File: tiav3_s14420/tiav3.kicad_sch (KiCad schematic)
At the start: 21 parts, among them J1 SSQ-103-01-G-D, J2 Conn_Coaxial, U1 OPA847IDBVT

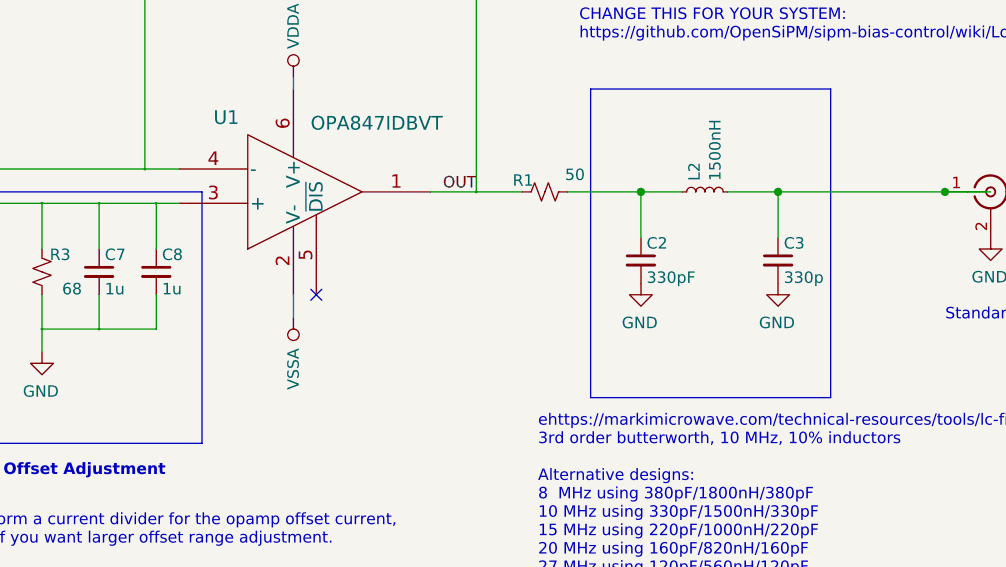
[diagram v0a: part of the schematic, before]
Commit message: Switch all TIA boards to 0603 for the low pass inductor
0402 is fine for higher cutoffs but its hard to find >1000nH in 0402 without having high resistance.
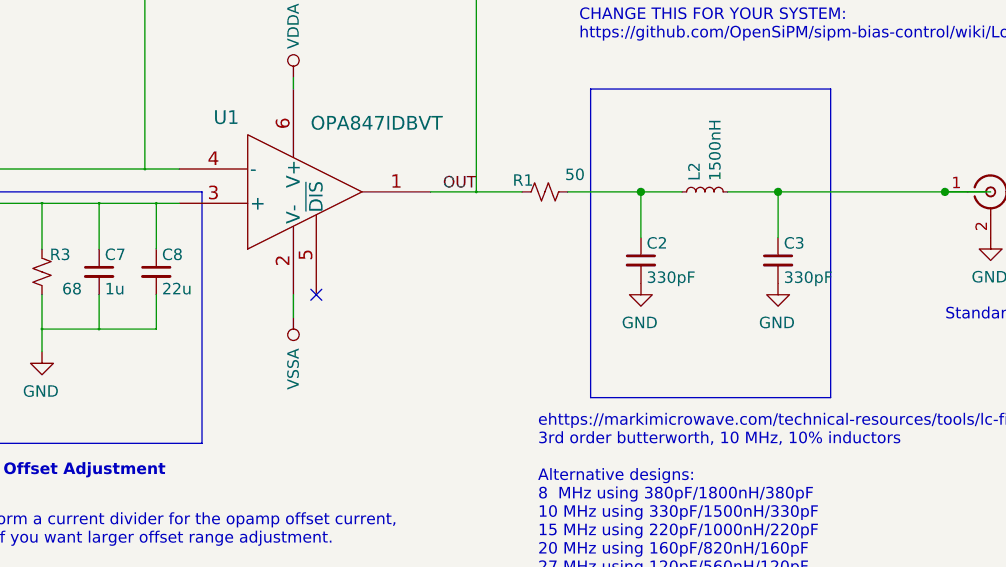
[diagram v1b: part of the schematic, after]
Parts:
- C1, C4: footprint Resistor_SMD:R_1206_3216Metric -> Capacitor_SMD:C_1206_3216Metric_Pad1.33x1.80mm_HandSolder
- C2: footprint Capacitor_SMD:C_0402_1005Metric -> Capacitor_SMD:C_0402_1005Metric_Pad0.74x0.62mm_HandSolder
- C3: value 330p -> 330pF; footprint Capacitor_SMD:C_0402_1005Metric -> Capacitor_SMD:C_0402_1005Metric_Pad0.74x0.62mm_HandSolder
- C8: value 1u -> 22u; footprint Capacitor_SMD:C_0402_1005Metric -> Capacitor_SMD:C_0603_1608Metric
- L2: footprint Inductor_SMD:L_0402_1005Metric -> Inductor_SMD:L_0603_1608Metric
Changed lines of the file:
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@@
 			)
 		)
-		(property "Footprint" "Resistor_SMD:R_1206_3216Metric"
+		(property "Footprint" "Capacitor_SMD:C_1206_3216Metric_Pad1.33x1.80mm_HandSolder"
 			(at 71.12 101.6 0)
 			(effects
@@
 			)
 		)
-		(property "Value" "1u"
+		(property "Value" "22u"
 			(at 172.085 121.285 0)
 			(effects
@@
 			)
 		)
-		(property "Footprint" "Capacitor_SMD:C_0402_1005Metric"
+		(property "Footprint" "Capacitor_SMD:C_0603_1608Metric"
 			(at 171.45 119.38 0)
 			(effects
@@
 			)
 		)
-		(property "Datasheet" " ~"
+		(property "Datasheet" "~"
 			(at 264.16 110.49 0)
 			(effects
@@
 			)
 		)
-		(property "Footprint" "Inductor_SMD:L_0402_1005Metric"
+		(property "Footprint" "Inductor_SMD:L_0603_1608Metric"
 			(at 232.41 110.49 0)
 			(effects
@@
 			)
 		)
-		(property "Footprint" "Capacitor_SMD:C_0402_1005Metric"
+		(property "Footprint" "Capacitor_SMD:C_0402_1005Metric_Pad0.74x0.62mm_HandSolder"
 			(at 225.298 118.11 0)
 			(effects
@@
 			)
 		)
-		(property "Footprint" "Resistor_SMD:R_1206_3216Metric"
+		(property "Footprint" "Capacitor_SMD:C_1206_3216Metric_Pad1.33x1.80mm_HandSolder"
 			(at 64.262 101.6 0)
 			(effects
@@
 			)
 		)
-		(property "Value" "330p"
+		(property "Value" "330pF"
 			(at 241.173 120.015 0)
 			(effects
@@
 			)
 		)
-		(property "Footprint" "Capacitor_SMD:C_0402_1005Metric"
+		(property "Footprint" "Capacitor_SMD:C_0402_1005Metric_Pad0.74x0.62mm_HandSolder"
 			(at 240.538 118.11 0)
 			(effects
